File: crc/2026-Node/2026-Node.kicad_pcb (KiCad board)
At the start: 2 copper layers, 32.6 x 83.4 mm, 24 parts, among them J1 Conn_01x02, J2 Conn_01x02, J3 Conn_01x04, J4 Conn_01x04, J5 Conn_01x04, J6 Conn_01x04, J7 Conn_01x04, J8 Conn_01x06, SW1 SW_MEC_5E, U1 STM32F446RETx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

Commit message: ノード完成
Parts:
- J4, J6: footprint Connector_JST:JST_XH_B4B-XH-A_1x04_P2.50mm_Vertical -> Connector_JST:JST_XH_S4B-XH-A_1x04_P2.50mm_Horizontal
- R4: value 120 -> R
- moved J6 14.0 mm to (152.4, 36.2), turned to 180 degrees
- moved J5 11.4 mm to (137.6, 43.6), turned to 180 degrees
- moved J3 7.75 mm to (152.4, 43.5), turned to 180 degrees
- moved J4 6.67 mm to (137.6, 36.3), turned to 180 degrees
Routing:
- net CAN1_L: track 54.4 -> 101.4 mm
- net CAN1_H: track 65.0 -> 21.0 mm
- net +5V: track 157.7 -> 175.3 mm

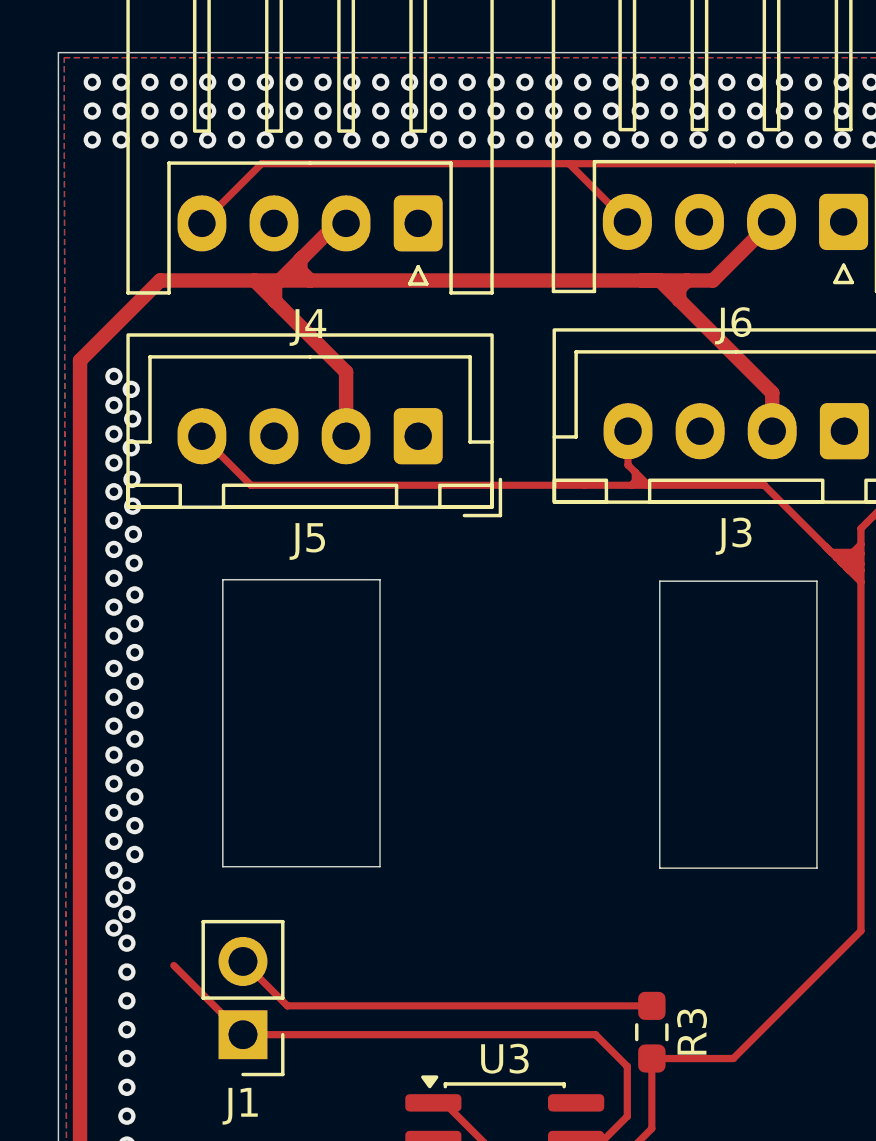
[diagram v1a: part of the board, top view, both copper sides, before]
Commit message: MD-SUB再設計多すぎだろFUCK！！！！！
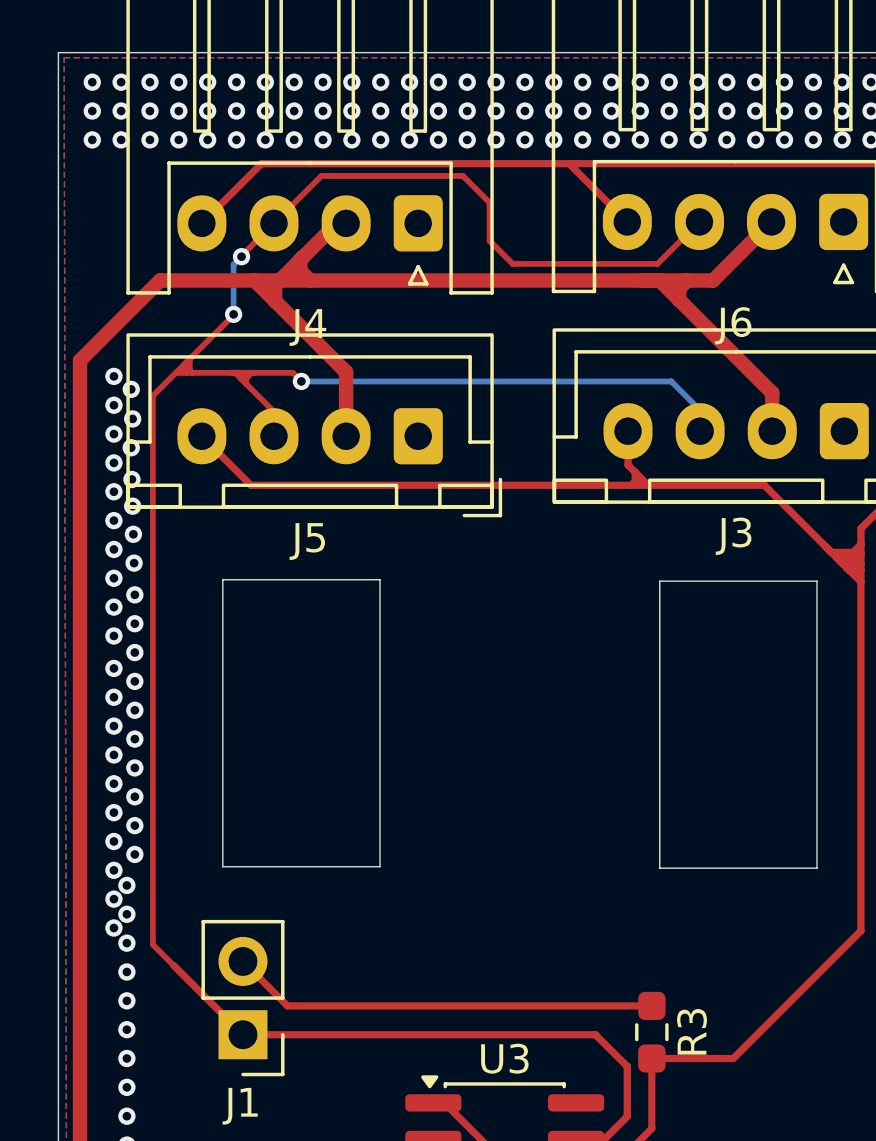
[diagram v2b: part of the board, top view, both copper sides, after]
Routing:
- net CAN1_H: track 21.0 -> 90.9 mm, vias 0 -> 3
